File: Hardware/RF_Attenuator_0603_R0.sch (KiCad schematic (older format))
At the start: 3 parts

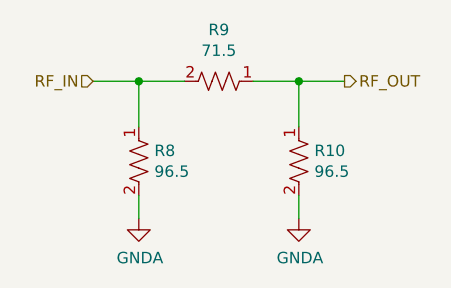
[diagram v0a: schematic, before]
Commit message: Major cleanup to both the schematic and directory structure. Stackup has changed accomodate to 0.65mm trace width. Chebyshev filter lived through the experience in the Qucs simulation; others not checked yet. I do want to re-visit the matching networks of all of the amplifiers as I have developed some good strategies to implement them.
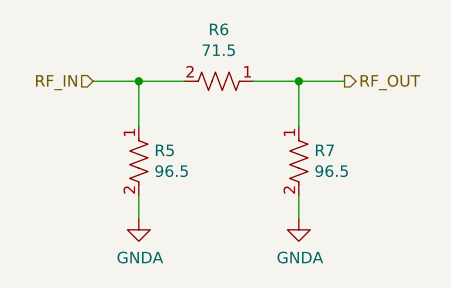
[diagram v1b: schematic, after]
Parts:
- renumbered R5 to R2, R6 to R3, R7 to R4
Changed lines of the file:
@@
 $Descr A4 11693 8268
 encoding utf-8
-Sheet 14 16
+Sheet 14 24
 Title ""
 Date ""
@@
 AR Path="/5F177657/5F203A7E/5F36A010" Ref="R?"  Part="1"
 AR Path="/5F177657/5F204141/5F36A010" Ref="R?"  Part="1"
-AR Path="/5F20B396/5F20D867/5F36A010" Ref="R5"  Part="1"
-AR Path="/5F20B396/5F20E71F/5F36A010" Ref="R8"  Part="1"
-F 0 "R8" H 5318 4046 50  0000 L CNN
+AR Path="/5F20B396/5F20D867/5F36A010" Ref="R2"  Part="1"
+AR Path="/5F20B396/5F20E71F/5F36A010" Ref="R5"  Part="1"
+F 0 "R5" H 5318 4046 50  0000 L CNN
 F 1 "RT0603DRE0796R5L" H 5300 3850 50  0001 L CNN
 F 2 "Resistor_SMD:R_0603_1608Metric" H 5250 4000 50  0001 C CNN
@@
 AR Path="/5F177657/5F203A7E/5F36A4D6" Ref="R?"  Part="1"
 AR Path="/5F177657/5F204141/5F36A4D6" Ref="R?"  Part="1"
-AR Path="/5F20B396/5F20D867/5F36A4D6" Ref="R7"  Part="1"
-AR Path="/5F20B396/5F20E71F/5F36A4D6" Ref="R10"  Part="1"
-F 0 "R10" H 6018 4046 50  0000 L CNN
+AR Path="/5F20B396/5F20D867/5F36A4D6" Ref="R4"  Part="1"
+AR Path="/5F20B396/5F20E71F/5F36A4D6" Ref="R7"  Part="1"
+F 0 "R7" H 6018 4046 50  0000 L CNN
 F 1 "RT0603DRE0796R5L" H 6000 3850 50  0001 L CNN
 F 2 "Resistor_SMD:R_0603_1608Metric" H 5950 4000 50  0001 C CNN
@@
 AR Path="/5F177657/5F203A7E/5F36A753" Ref="R?"  Part="1"
 AR Path="/5F177657/5F204141/5F36A753" Ref="R?"  Part="1"
-AR Path="/5F20B396/5F20D867/5F36A753" Ref="R6"  Part="1"
-AR Path="/5F20B396/5F20E71F/5F36A753" Ref="R9"  Part="1"
-F 0 "R9" V 5375 3650 50  0000 C CNN
+AR Path="/5F20B396/5F20D867/5F36A753" Ref="R3"  Part="1"
+AR Path="/5F20B396/5F20E71F/5F36A753" Ref="R6"  Part="1"
+F 0 "R6" V 5375 3650 50  0000 C CNN
 F 1 "RT0603BRD0771R5L" H 6025 3500 50  0001 C CNN
 F 2 "Resistor_SMD:R_0603_1608Metric" H 5600 3650 50  0001 C CNN
@@
 AR Path="/5F177657/5F203A7E/5F2183E0" Ref="#PWR?"  Part="1"
 AR Path="/5F177657/5F204141/5F2183E0" Ref="#PWR?"  Part="1"
-AR Path="/5F20B396/5F20D867/5F2183E0" Ref="#PWR054"  Part="1"
-AR Path="/5F20B396/5F20E71F/5F2183E0" Ref="#PWR056"  Part="1"
-F 0 "#PWR056" H 5950 4000 50  0001 C CNN
+AR Path="/5F20B396/5F20D867/5F2183E0" Ref="#PWR020"  Part="1"
+AR Path="/5F20B396/5F20E71F/5F2183E0" Ref="#PWR022"  Part="1"
+F 0 "#PWR022" H 5950 4000 50  0001 C CNN
 F 1 "GNDA" H 5955 4077 50  0000 C CNN
 F 2 "" H 5950 4250 50  0001 C CNN
@@
 AR Path="/5F177657/5F203A7E/5F2183E1" Ref="#PWR?"  Part="1"
 AR Path="/5F177657/5F204141/5F2183E1" Ref="#PWR?"  Part="1"
-AR Path="/5F20B396/5F20D867/5F2183E1" Ref="#PWR053"  Part="1"
-AR Path="/5F20B396/5F20E71F/5F2183E1" Ref="#PWR055"  Part="1"
-F 0 "#PWR055" H 5250 4000 50  0001 C CNN
+AR Path="/5F20B396/5F20D867/5F2183E1" Ref="#PWR019"  Part="1"
+AR Path="/5F20B396/5F20E71F/5F2183E1" Ref="#PWR021"  Part="1"
+F 0 "#PWR021" H 5250 4000 50  0001 C CNN
 F 1 "GNDA" H 5255 4077 50  0000 C CNN
 F 2 "" H 5250 4250 50  0001 C CNN
